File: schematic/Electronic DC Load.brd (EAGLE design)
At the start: 100 x 51.5 mm, 104 parts, among them J1 POWER_JACKPTH_LOCK, J2 AVR_SPI_PROG_3X2PTH, J3 FAN, J4 KF762-2, Q1 16MHz, Q2 IRFP250NV, Q3 600mA/40V, U1 AMS1117-5.0, U10 AD8629ARZ, U2 REF5050_D_8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

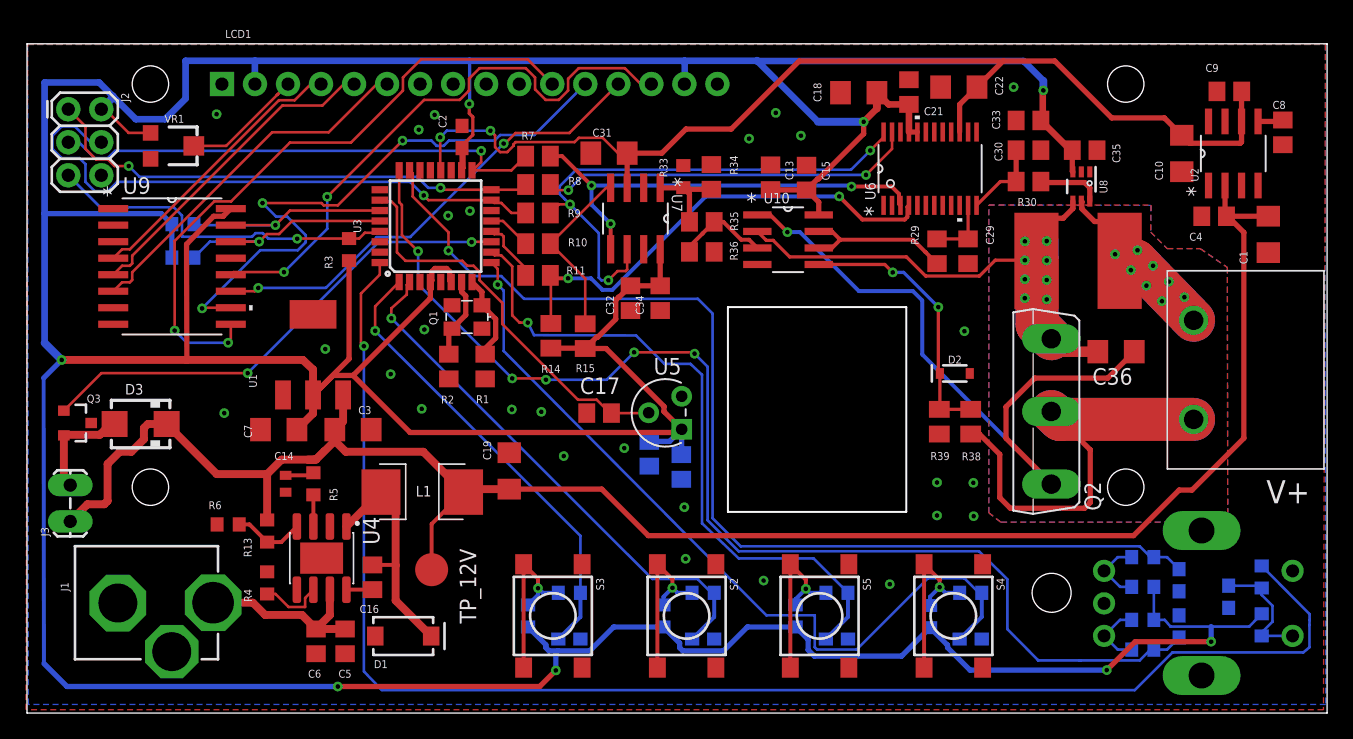
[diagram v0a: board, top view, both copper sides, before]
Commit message: Fixed capacitors packages
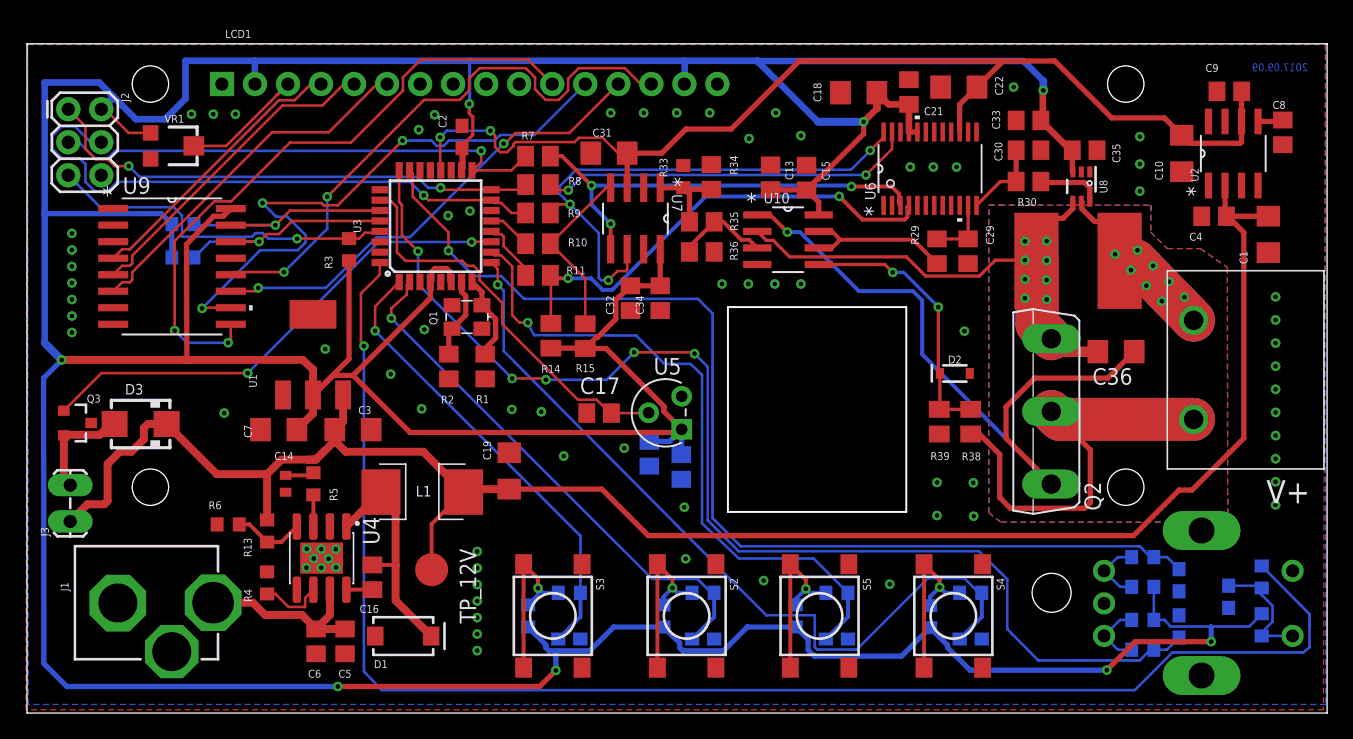
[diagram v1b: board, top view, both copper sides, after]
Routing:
- net GND: vias 27 -> 75
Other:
- board text added: "2017.09.09"
- board text added: "Electronic Load By XJ 2017.09"
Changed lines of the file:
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@@
 <setting verticaltext="up"/>
 </settings>
-<grid distance="50" unitdist="mil" unit="mil" style="lines" multiple="1" display="no" altdistance="1" altunitdist="mil" altunit="mil"/>
+<grid distance="50" unitdist="mil" unit="mm" style="lines" multiple="1" display="no" altdistance="1" altunitdist="mil" altunit="mil"/>
 <layers>
 <layer number="1" name="Top" color="4" fill="1" visible="yes" active="yes"/>
@@
 <wire x1="78.74" y1="28.956" x2="78.7654" y2="28.9814" width="0.4064" layer="48"/>
 <text x="95.3008" y="16.129" size="1.778" layer="21">V+</text>
+<text x="97.3328" y="38.1762" size="1.778" layer="22" font="vector" rot="MR0">Electronic Load
+By XJ
+2017.09</text>
+<text x="98.5012" y="49.3522" size="0.6096" layer="16" font="vector" ratio="15" rot="MR0">2017.09.09</text>
+<circle x="-11.1506" y="16.6116" radius="2.620265625" width="0.2" layer="47"/>
 </plain>
 <attributes>
@@
 <wire x1="83.9216" y1="37.7952" x2="84.0228" y2="37.694" width="0.4064" layer="1"/>
 <wire x1="84.0228" y1="37.694" x2="84.0228" y2="34.7726" width="0.4064" layer="1"/>
-<via x="14.5796" y="46.0502" extent="1-16" drill="0.35"/>
+<via x="14.3256" y="46.0502" extent="1-16" drill="0.35"/>
 <via x="30.1244" y="44.8564" extent="1-16" drill="0.35"/>
 <via x="34.0614" y="38.608" extent="1-16" drill="0.35"/>
@@
 <via x="72.0852" y="29.3624" extent="1-16" drill="0.35"/>
 <via x="39.5478" y="23.1648" extent="1-16" drill="0.35"/>
+<via x="52.5018" y="46.1518" extent="1-16" drill="0.35"/>
+<via x="49.9618" y="46.1518" extent="1-16" drill="0.35"/>
+<via x="47.4218" y="46.1518" extent="1-16" drill="0.35"/>
+<via x="44.8818" y="46.1518" extent="1-16" drill="0.35"/>
+<via x="16.0274" y="46.0502" extent="1-16" drill="0.35"/>
+<via x="12.6492" y="46.0502" extent="1-16" drill="0.35"/>
+<via x="3.4544" y="36.8808" extent="1-16" drill="0.35"/>
+<via x="3.4544" y="35.6108" extent="1-16" drill="0.35"/>
+<via x="3.4544" y="34.3408" extent="1-16" drill="0.35"/>
+<via x="3.4544" y="33.0708" extent="1-16" drill="0.35"/>
+<via x="3.4544" y="31.8008" extent="1-16" drill="0.35"/>
+<via x="3.4544" y="30.5308" extent="1-16" drill="0.35"/>
+<via x="3.4544" y="29.2608" extent="1-16" drill="0.35"/>
+<via x="96.012" y="32.004" extent="1-16" drill="0.35"/>
+<via x="96.012" y="30.226" extent="1-16" drill="0.35"/>
+<via x="96.012" y="28.448" extent="1-16" drill="0.35"/>
+<via x="96.012" y="26.67" extent="1-16" drill="0.35"/>
+<via x="96.012" y="24.892" extent="1-16" drill="0.35"/>
+<via x="96.012" y="23.114" extent="1-16" drill="0.35"/>
+<via x="96.012" y="21.336" extent="1-16" drill="0.35"/>
+<via x="96.012" y="19.558" extent="1-16" drill="0.35"/>
+<via x="96.012" y="17.78" extent="1-16" drill="0.35"/>
+<via x="96.012" y="16.002" extent="1-16" drill="0.35"/>
+<via x="34.6202" y="12.4206" extent="1-16" drill="0.35"/>
+<via x="34.6202" y="11.1506" extent="1-16" drill="0.35"/>
+<via x="34.6202" y="9.8806" extent="1-16" drill="0.35"/>
+<via x="34.6202" y="8.6106" extent="1-16" drill="0.35"/>
+<via x="34.6202" y="7.3406" extent="1-16" drill="0.35"/>
+<via x="34.6202" y="6.0706" extent="1-16" drill="0.35"/>
+<via x="34.6202" y="4.8006" extent="1-16" drill="0.35"/>
+<via x="85.5726" y="44.323" extent="1-16" drill="0.35"/>
+<via x="85.5726" y="42.2148" extent="1-16" drill="0.35"/>
+<via x="85.5726" y="40.132" extent="1-16" drill="0.35"/>
+<via x="67.9196" y="41.9862" extent="1-16" drill="0.35"/>
+<via x="69.6976" y="41.9862" extent="1-16" drill="0.35"/>
+<via x="71.4756" y="41.9862" extent="1-16" drill="0.35"/>
+<via x="53.4416" y="32.9946" extent="1-16" drill="0.35"/>
+<via x="55.4736" y="32.9946" extent="1-16" drill="0.35"/>
+<via x="57.5056" y="32.9946" extent="1-16" drill="0.35"/>
+<via x="59.5122" y="32.9946" extent="1-16" drill="0.35"/>
+<via x="21.5138" y="12.6238" extent="1-16" drill="0.35"/>
+<via x="22.6314" y="12.5984" extent="1-16" drill="0.35"/>
+<via x="23.749" y="12.5984" extent="1-16" drill="0.35"/>
+<via x="22.0472" y="11.8872" extent="1-16" drill="0.35"/>
+<via x="23.1902" y="11.8618" extent="1-16" drill="0.35"/>
+<via x="21.4884" y="11.176" extent="1-16" drill="0.35"/>
+<via x="22.6314" y="11.176" extent="1-16" drill="0.35"/>
+<via x="23.7744" y="11.2014" extent="1-16" drill="0.35"/>
 </signal>
 <signal name="N$11">
@@
 <wire x1="31.0198" y1="31.9033875" x2="25.0752125" y2="25.9588" width="0.4064" layer="1"/>
 <wire x1="2.667" y1="27.1526" x2="1.279696875" y2="25.765296875" width="0.4064" layer="16"/>
-<wire x1="1.279696875" y1="25.765296875" x2="1.301653125" y2="3.81066875" width="0.3048" layer="16"/>
+<wire x1="1.279696875" y1="25.765296875" x2="1.301653125" y2="3.81066875" width="0.4064" layer="16"/>
 <wire x1="1.301653125" y1="3.81066875" x2="3.073721875" y2="2.0386" width="0.4064" layer="16"/>
 <wire x1="3.073721875" y1="2.0386" x2="23.9014" y2="2.0386" width="0.4064" layer="16"/>
@@
 </drawing>
 <compatibility>
+<note version="6.3" minversion="6.2.2" severity="warning">
+Since Version 6.2.2 text objects can contain more than one line,
+which will not be processed correctly with this version.
+</note>
 <note version="8.2" severity="warning">
 Since Version 8.2, EAGLE supports online libraries. The ids
